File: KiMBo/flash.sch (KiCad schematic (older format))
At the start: 31 parts, among them IC1 24LC32AT-I/OT, U2 OSD3358, U6 74LVC1G06, U7 EMMC**G-S100

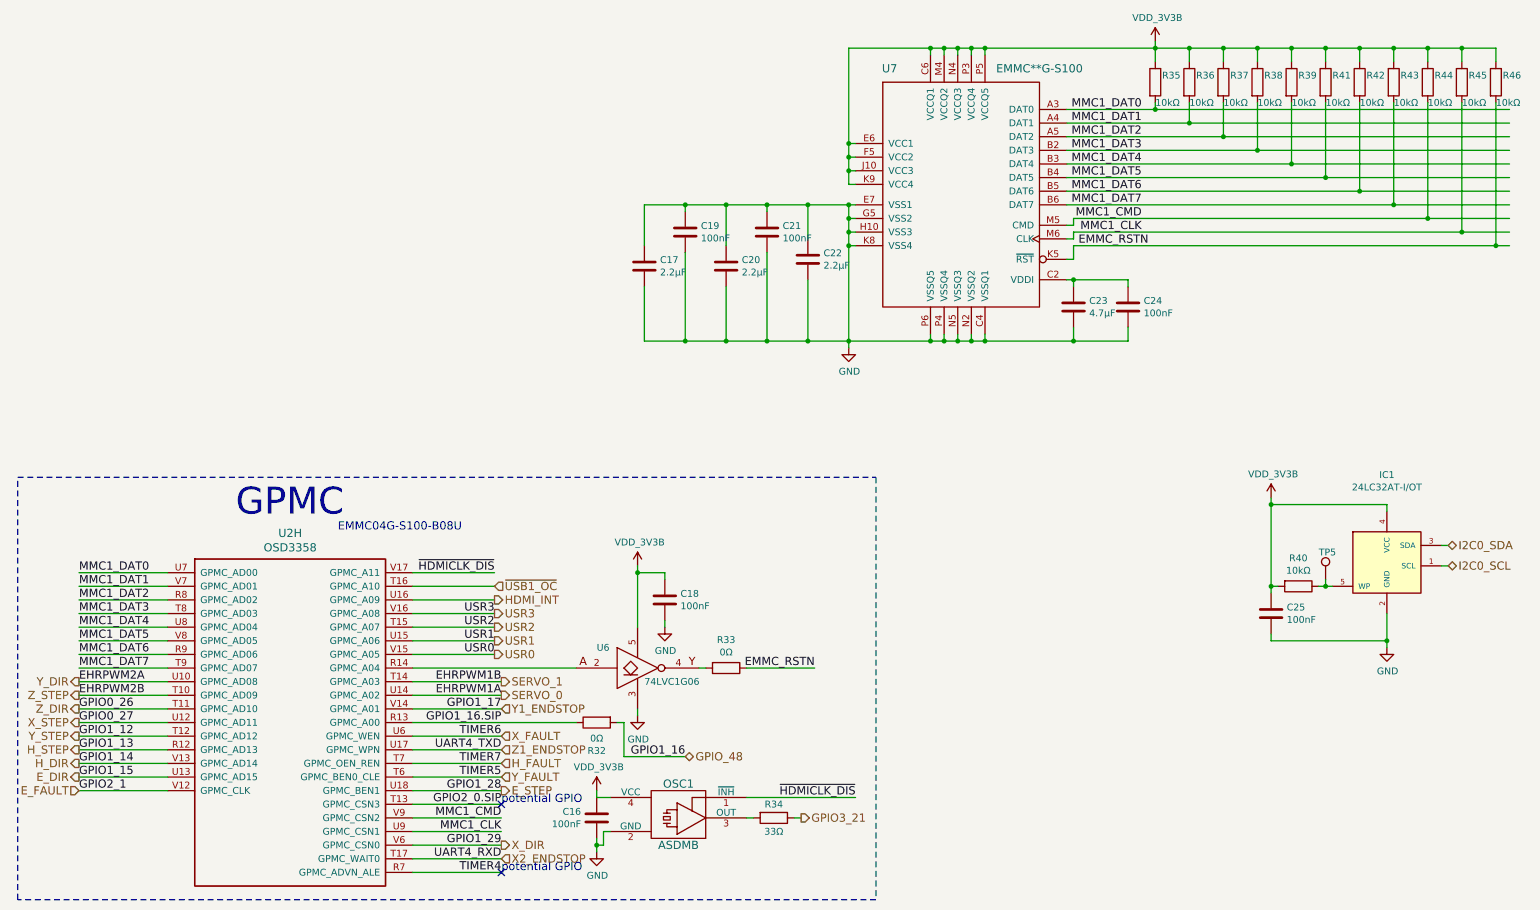
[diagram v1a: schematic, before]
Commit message: Leave SPI0 free for a display, reassign pins so SPI1 is available
Fix some typos/errors
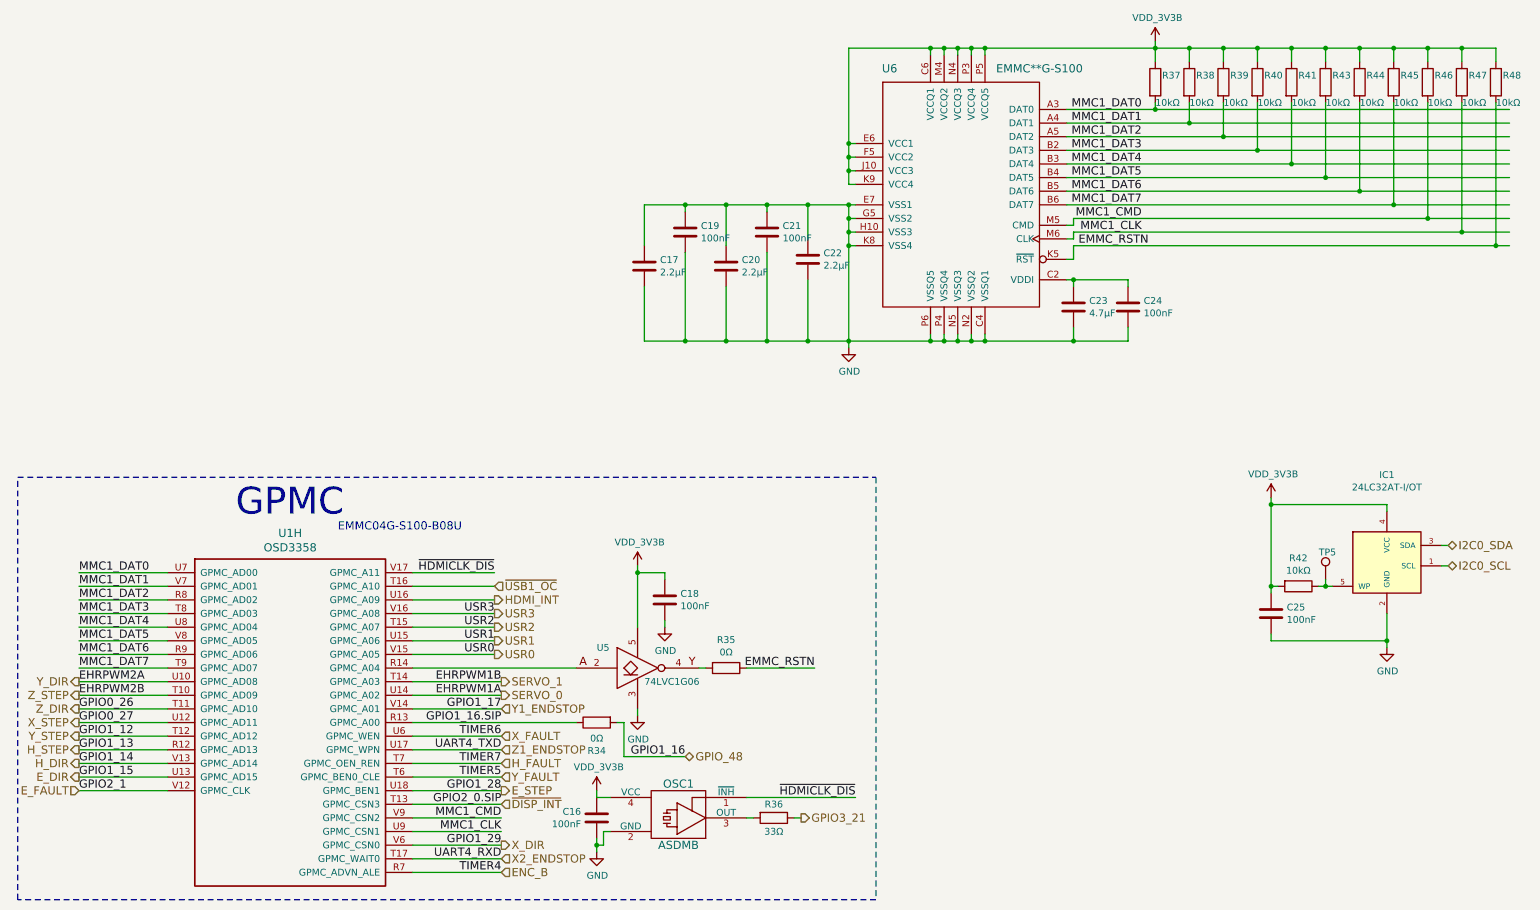
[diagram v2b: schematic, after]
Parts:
- renumbered R32 to R34, R33 to R35, R34 to R36, R35 to R37, R36 to R38, R37 to R39, R38 to R40, R39 to R41, R40 to R42, R41 to R43, R42 to R44, R43 to R45, R44 to R46, R45 to R47, R46 to R48, U2 to U1, U6 to U5, U7 to U6
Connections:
- net labels added: ENC_B, ~DISP_INT
- no-connect marks 2 -> 0
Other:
- note removed: "potential GPIO"
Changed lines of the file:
@@
 $EndDescr
 $Comp
-L R R35
+L R R37
 U 1 1 58938DE0
 P 10550 2900
-F 0 "R35" H 10600 2950 50  0000 L CNN
+F 0 "R37" H 10600 2950 50  0000 L CNN
 F 1 "10kΩ" H 10550 2750 50  0000 L CNN
 F 2 "Resistors_SMD:R_0402" V 10480 2900 50  0001 C CNN
@@
 $EndComp
 $Comp
-L R R36
+L R R38
 U 1 1 58938E26
 P 10800 2900
-F 0 "R36" H 10850 2950 50  0000 L CNN
+F 0 "R38" H 10850 2950 50  0000 L CNN
 F 1 "10kΩ" H 10800 2750 50  0000 L CNN
 F 2 "Resistors_SMD:R_0402" V 10730 2900 50  0001 C CNN
@@
 $EndComp
 $Comp
-L R R37
+L R R39
 U 1 1 58938E51
 P 11050 2900
-F 0 "R37" H 11100 2950 50  0000 L CNN
+F 0 "R39" H 11100 2950 50  0000 L CNN
 F 1 "10kΩ" H 11050 2750 50  0000 L CNN
 F 2 "Resistors_SMD:R_0402" V 10980 2900 50  0001 C CNN
@@
 $EndComp
 $Comp
-L R R38
+L R R40
 U 1 1 58938E75
 P 11300 2900
-F 0 "R38" H 11350 2950 50  0000 L CNN
+F 0 "R40" H 11350 2950 50  0000 L CNN
 F 1 "10kΩ" H 11300 2750 50  0000 L CNN
 F 2 "Resistors_SMD:R_0402" V 11230 2900 50  0001 C CNN
@@
 $EndComp
 $Comp
-L R R39
+L R R41
 U 1 1 58938EA0
 P 11550 2900
-F 0 "R39" H 11600 2950 50  0000 L CNN
+F 0 "R41" H 11600 2950 50  0000 L CNN
 F 1 "10kΩ" H 11550 2750 50  0000 L CNN
 F 2 "Resistors_SMD:R_0402" V 11480 2900 50  0001 C CNN
@@
 $EndComp
 $Comp
-L R R41
+L R R43
 U 1 1 58938F20
 P 11800 2900
-F 0 "R41" H 11850 2950 50  0000 L CNN
+F 0 "R43" H 11850 2950 50  0000 L CNN
 F 1 "10kΩ" H 11800 2750 50  0000 L CNN
 F 2 "Resistors_SMD:R_0402" V 11730 2900 50  0001 C CNN
@@
 	9300 4800 9300 4750
 $Comp
-L R R42
+L R R44
 U 1 1 5893A6C3
 P 12050 2900
-F 0 "R42" H 12100 2950 50  0000 L CNN
+F 0 "R44" H 12100 2950 50  0000 L CNN
 F 1 "10kΩ" H 12050 2750 50  0000 L CNN
 F 2 "Resistors_SMD:R_0402" V 11980 2900 50  0001 C CNN
@@
 $EndComp
 $Comp
-L R R43
+L R R45
 U 1 1 5893A6FB
 P 12300 2900
-F 0 "R43" H 12350 2950 50  0000 L CNN
+F 0 "R45" H 12350 2950 50  0000 L CNN
 F 1 "10kΩ" H 12300 2750 50  0000 L CNN
 F 2 "Resistors_SMD:R_0402" V 12230 2900 50  0001 C CNN
@@
 $EndComp
 $Comp
-L R R44
+L R R46
 U 1 1 5893A736
 P 12550 2900
-F 0 "R44" H 12600 2950 50  0000 L CNN
+F 0 "R46" H 12600 2950 50  0000 L CNN
 F 1 "10kΩ" H 12550 2750 50  0000 L CNN
 F 2 "Resistors_SMD:R_0402" V 12480 2900 50  0001 C CNN
@@
 	10550 3100 10550 3050
 $Comp
-L R R45
+L R R47
 U 1 1 5893AC56
 P 12800 2900
-F 0 "R45" H 12850 2950 50  0000 L CNN
+F 0 "R47" H 12850 2950 50  0000 L CNN
 F 1 "10kΩ" H 12800 2750 50  0000 L CNN
 F 2 "Resistors_SMD:R_0402" V 12730 2900 50  0001 C CNN
@@
 $EndComp
 $Comp
-L R R46
+L R R48
 U 1 1 5893AC8F
 P 13050 2900
-F 0 "R46" H 13100 2950 50  0000 L CNN
+F 0 "R48" H 13100 2950 50  0000 L CNN
 F 1 "10kΩ" H 13050 2750 50  0000 L CNN
 F 2 "Resistors_SMD:R_0402" V 12980 2900 50  0001 C CNN
@@
 Connection ~ 12800 2650
 $Comp
-L GND #PWR098
+L GND #PWR097
 U 1 1 5893C2D6
 P 8300 4850
-F 0 "#PWR098" H 8300 4600 50  0001 C CNN
+F 0 "#PWR097" H 8300 4600 50  0001 C CNN
 F 1 "GND" H 8305 4677 50  0000 C CNN
 F 2 "" H 8300 4850 50  0000 C CNN
@@
 $EndComp
 $Comp
-L R R40
+L R R42
 U 1 1 589CA43D
 P 11600 6600
-F 0 "R40" V 11393 6600 50  0000 C CNN
+F 0 "R42" V 11393 6600 50  0000 C CNN
 F 1 "10kΩ" V 11484 6600 50  0000 C CNN
 F 2 "Resistors_SMD:R_0402" V 11530 6600 50  0001 C CNN
@@
 	11400 7000 11400 6950
 $Comp
-L GND #PWR099
+L GND #PWR098
 U 1 1 589CAA98
 P 12250 7050
-F 0 "#PWR099" H 12250 6800 50  0001 C CNN
+F 0 "#PWR098" H 12250 6800 50  0001 C CNN
 F 1 "GND" H 12255 6877 50  0000 C CNN
 F 2 "" H 12250 7050 50  0000 C CNN
@@
 P 3300 6500
 AR Path="/581AEC7B/58ED6372" Ref="U?"  Part="8"
-AR Path="/581A9CCF/58ED6372" Ref="U2"  Part="8"
-F 0 "U2" H 4200 6790 60  0000 C CNN
+AR Path="/581A9CCF/58ED6372" Ref="U1"  Part="8"
+F 0 "U1" H 4200 6790 60  0000 C CNN
 F 1 "OSD3358" H 4200 6684 60  0000 C CNN
 F 2 "" H 3300 6500 60  0001 C CNN
@@
 GPIO1_16.SIP
 $Comp
-L R R32
+L R R34
 U 1 1 58ED6392
 P 6450 7600
-F 0 "R32" V 6657 7600 50  0000 C CNN
+F 0 "R34" V 6657 7600 50  0000 C CNN
 F 1 "0Ω" V 6566 7600 50  0000 C CNN
 F 2 "Resistors_SMD:R_0402" V 6380 7600 50  0001 C CNN
@@
 GPIO2_0.SIP
 $Comp
-L 74LVC1G06 U6
+L 74LVC1G06 U5
 U 1 1 58ED639E
 P 6750 7200
-F 0 "U6" H 6450 7350 50  0000 L CNN
+F 0 "U5" H 6450 7350 50  0000 L CNN
 F 1 "74LVC1G06" H 6800 7100 50  0000 L CNN
 F 2 "" H 6750 7200 50  0001 C CNN
@@
 $EndComp
 $Comp
-L GND #PWR0100
+L GND #PWR099
 U 1 1 58ED63A5
 P 6750 7550
-F 0 "#PWR0100" H 6750 7300 50  0001 C CNN
+F 0 "#PWR099" H 6750 7300 50  0001 C CNN
 F 1 "GND" H 6755 7377 50  0000 C CNN
 F 2 "" H 6750 7550 50  0000 C CNN
@@
 $EndComp
 $Comp
-L GND #PWR0101
+L GND #PWR0100
 U 1 1 58ED63B8
 P 6950 6900
-F 0 "#PWR0101" H 6950 6650 50  0001 C CNN
+F 0 "#PWR0100" H 6950 6650 50  0001 C CNN
 F 1 "GND" H 6955 6727 50  0000 C CNN
 F 2 "" H 6950 6900 50  0000 C CNN
@@
 $EndComp
 $Comp
-L R R33
+L R R35
 U 1 1 58ED63BE
 P 7400 7200
-F 0 "R33" V 7193 7200 50  0000 C CNN
+F 0 "R35" V 7193 7200 50  0000 C CNN
 F 1 "0Ω" V 7284 7200 50  0000 C CNN
 F 2 "Resistors_SMD:R_0402" V 7330 7200 50  0001 C CNN
@@
 $EndComp
 $Comp
-L GND #PWR0102
+L GND #PWR0101
 U 1 1 58ED63D4
 P 6450 8550
-F 0 "#PWR0102" H 6450 8300 50  0001 C CNN
+F 0 "#PWR0101" H 6450 8300 50  0001 C CNN
 F 1 "GND" H 6455 8377 50  0000 C CNN
 F 2 "" H 6450 8550 50  0000 C CNN
@@
 $EndComp
 $Comp
-L R R34
+L R R36
 U 1 1 58ED63E0
 P 7750 8300
-F 0 "R34" V 7650 8300 50  0000 C CNN
+F 0 "R36" V 7650 8300 50  0000 C CNN
 F 1 "33Ω" V 7850 8300 50  0000 C CNN
 F 2 "" V 7680 8300 50  0001 C CNN
@@
 MMC1_CLK
 $Comp
-L EMMC**G-S100 U7
+L EMMC**G-S100 U6
 U 1 1 5893814B
 P 9150 3750
-F 0 "U7" H 8600 4700 60  0000 C CNN
+F 0 "U6" H 8600 4700 60  0000 C CNN
 F 1 "EMMC**G-S100" H 9700 4700 60  0000 C CNN
 F 2 "" H 9150 4250 60  0001 C CNN
@@
 SERVO_0
 $Comp
-L VDD_3V3B #PWR0103
+L VDD_3V3B #PWR0102
 U 1 1 59E9BAE0
 P 10550 2600
-F 0 "#PWR0103" H 10550 2450 50  0001 C CNN
+F 0 "#PWR0102" H 10550 2450 50  0001 C CNN
 F 1 "VDD_3V3B" H 10565 2773 50  0000 C CNN
 F 2 "" H 10550 2600 50  0000 C CNN
@@
 USR0
 $Comp
-L VDD_3V3B #PWR0104
+L VDD_3V3B #PWR0103
 U 1 1 59FAFB00
 P 6450 8100
-F 0 "#PWR0104" H 6450 7950 50  0001 C CNN
+F 0 "#PWR0103" H 6450 7950 50  0001 C CNN
 F 1 "VDD_3V3B" H 6465 8273 50  0000 C CNN
 F 2 "" H 6450 8100 50  0000 C CNN
@@
 $EndComp
 $Comp
-L VDD_3V3B #PWR0105
+L VDD_3V3B #PWR0104
 U 1 1 59FBC4DE
 P 6750 6450
-F 0 "#PWR0105" H 6750 6300 50  0001 C CNN
+F 0 "#PWR0104" H 6750 6300 50  0001 C CNN
 F 1 "VDD_3V3B" H 6765 6623 50  0000 C CNN
 F 2 "" H 6750 6450 50  0000 C CNN
@@
 Connection ~ 11400 6600
 $Comp
-L VDD_3V3B #PWR0106
+L VDD_3V3B #PWR0105
 U 1 1 59FBD7EE
 P 11400 5950
-F 0 "#PWR0106" H 11400 5800 50  0001 C CNN
+F 0 "#PWR0105" H 11400 5800 50  0001 C CNN
 F 1 "VDD_3V3B" H 11415 6123 50  0000 C CNN
 F 2 "" H 11400 5950 50  0000 C CNN
@@
 $EndComp
 Connection ~ 11400 6000
-Text Notes 5750 8200 0    60   ~ 0
-potential GPIO
-Text Notes 5750 8700 0    60   ~ 0
-potential GPIO
 Text HLabel 12700 6300 2    60   BiDi ~ 0
 I2C0_SDA
 Text HLabel 12700 6450 2    60   BiDi ~ 0
 I2C0_SCL
-NoConn ~ 5750 8700
-NoConn ~ 5750 8200
 Text HLabel 5700 6700 2    60   Output ~ 0
 HDMI_INT
@@
 	1    0    0    -1
 $EndComp
+Text HLabel 5750 8700 2    60   Input ~ 0
+ENC_B
+Text HLabel 5750 8200 2    60   Input ~ 0
+~DISP_INT
 $EndSCHEMATC
